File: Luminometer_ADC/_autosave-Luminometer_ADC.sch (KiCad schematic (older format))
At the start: 39 parts, among them J9 Conn_01x08, U1 LP5907MFX-4.5, U2 ADS131M08IPBS, U3 LP5907MFX-3, U4 ADR512, Y1 CSTNE8M19

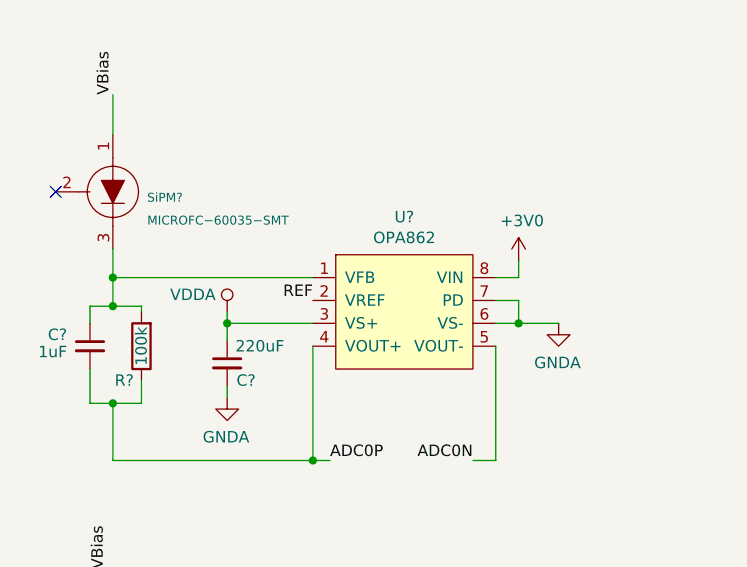
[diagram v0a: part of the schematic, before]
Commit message: Started dev on SiPM version
Shifting to a two-channel, single-board design in response to discussions with our collaborators. Notes:
- Switching to MICROFC−60035−SMT sensor, which should be able to detect 1 fM nanoluc in 1-10 seconds, from back of envelope calculations
- Keeping the 8-channel ADC chosen by Robert
- We will need to move away from the OPA862 (not done yet) due to its poor performance at DC (bias offset and its temperature dependence is unacceptable)
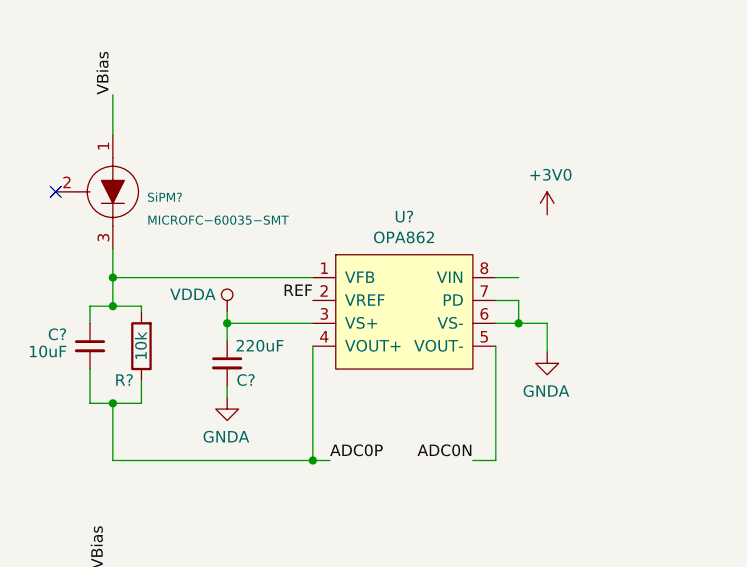
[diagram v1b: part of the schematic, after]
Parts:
- C?: value 1uF -> 10uF
- R?: value 100k -> 10k
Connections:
- net +3V0: no longer U?.8 (VIN)
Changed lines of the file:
@@
 P 1300 2600
 F 0 "R?" H 1375 2750 50  0000 C CNN
-F 1 "100k" V 1300 2600 50  0000 C CNN
+F 1 "10k" V 1300 2600 50  0000 C CNN
 F 2 "Resistor_SMD:R_0603_1608Metric" V 1230 2600 50  0001 C CNN
 F 3 "~" H 1300 2600 50  0001 C CNN
@@
 P 1075 2600
 F 0 "C?" H 1175 2650 50  0000 L CNN
-F 1 "1uF" H 1175 2575 50  0000 L CNN
+F 1 "10uF" H 1175 2575 50  0000 L CNN
 F 2 "Capacitor_SMD:C_0603_1608Metric" H 1075 2600 50  0001 C CNN
 F 3 "~" H 1075 2600 50  0001 C CNN
@@
 L power:GNDA #PWR?
 U 1 1 5F817AD9
-P 3125 2500
-F 0 "#PWR?" H 3125 2250 50  0001 C CNN
-F 1 "GNDA" H 3130 2327 50  0000 C CNN
-F 2 "" H 3125 2500 50  0001 C CNN
-F 3 "" H 3125 2500 50  0001 C CNN
-	1    3125 2500
+P 3075 2625
+F 0 "#PWR?" H 3075 2375 50  0001 C CNN
+F 1 "GNDA" H 3080 2452 50  0000 C CNN
+F 2 "" H 3075 2625 50  0001 C CNN
+F 3 "" H 3075 2625 50  0001 C CNN
+	1    3075 2625
 	-1   0    0    -1
 $EndComp
@@
 Wire Wire Line
 	2950 2400 2950 2500
-Connection ~ 2950 2500
-Wire Wire Line
-	2950 2500 3125 2500
 $Comp
 L power:+3V0 #PWR?
 U 1 1 5F8315C3
-P 2950 2225
-F 0 "#PWR?" H 2950 2075 50  0001 C CNN
-F 1 "+3V0" H 2965 2398 50  0000 C CNN
-F 2 "" H 2950 2225 50  0001 C CNN
-F 3 "" H 2950 2225 50  0001 C CNN
-	1    2950 2225
-	1    0    0    -1
-$EndComp
-Wire Wire Line
-	2950 2225 2950 2300
+P 3075 2025
+F 0 "#PWR?" H 3075 1875 50  0001 C CNN
+F 1 "+3V0" H 3090 2198 50  0000 C CNN
+F 2 "" H 3075 2025 50  0001 C CNN
+F 3 "" H 3075 2025 50  0001 C CNN
+	1    3075 2025
+	1    0    0    -1
+$EndComp
 Wire Wire Line
 	2950 2300 2850 2300
@@
 Wire Wire Line
 	1175 2850 1300 2850
+Wire Wire Line
+	2950 2500 3075 2500
+Wire Wire Line
+	3075 2500 3075 2625
+Connection ~ 2950 2500
 $EndSCHEMATC
